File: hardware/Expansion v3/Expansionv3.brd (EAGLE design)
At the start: 89.2 x 36.7 mm, 44 parts, among them IC1 PIC18F2480-I/SP, J1 USB1035-XX-X-X-X-B_REVE, T1 BC547, T2 BC547, T3 BC547, T4 BC547, U1 IR3315, U2 IR3315, U3 IR3315, U4 IR3315

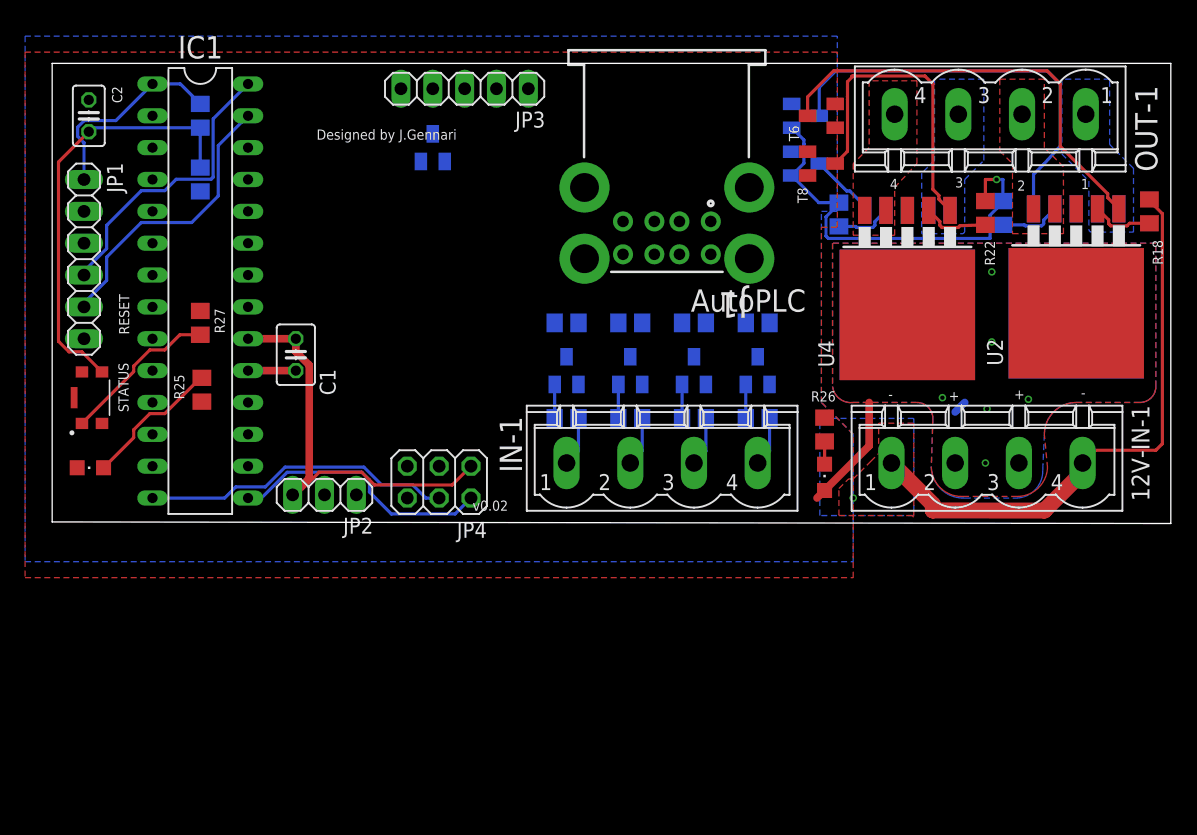
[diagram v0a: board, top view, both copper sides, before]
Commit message: Added ext board
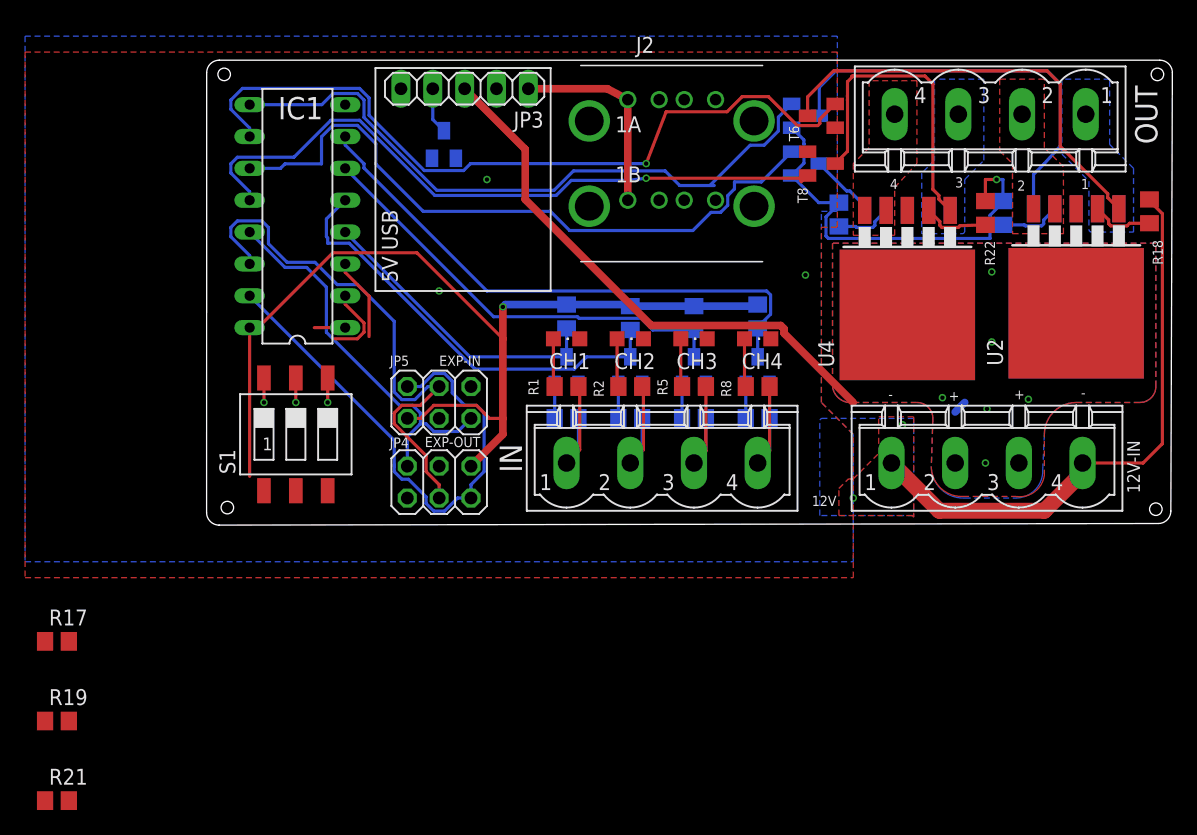
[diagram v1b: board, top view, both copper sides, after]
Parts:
- removed C1: 0.1uF, resistor:C025-030X050
- removed C2: 100nF, resistor:C025-025X050
- removed J1: USB1035-XX-X-X-X-B_REVE, USB1035-XX-X-X-X-B_REVE:GCT_USB1035-XX-X-X-X-B_REVE
- removed JP1: ICSP, pinhead:1X06
- removed JP2: 5V REG, pinhead:1X03
- removed LED10: (no value), led:CHIPLED_0805
- removed LED9: STATUS, led:CHIPLED_0805
- removed R24, R3: 10k, resistor:R0805
- removed R25: 150R, resistor:R0805
- removed R26: (no value), resistor:R0805
- removed R27: 100R, resistor:R0805
- added J2: (no value), InputOutputIO (rev17e):614008235023
- added JP5: (no value), pinhead:2X03
- added LED1, LED2, LED3, LED5: (no value), led:CHIPLED_0805
- added R1, R17, R19, R2, R21, R5, R8: (no value), resistor:R0805
- IC1: value PIC18F2480-I/SP -> PCF8574P; device microchip:DIL28-3 -> micro-philips:DIL16
- S1: value KMR421GULCLFS -> SWS003; device KMR421GULCLFS:SW_KMR421GULCLFS -> smd-special:SMS-003
- moved S1 16.5 mm to (43.2, 20.3), turned to 0 degrees
- moved IC1 9.78 mm to (43.3, 37.7), turned to 90 degrees
- moved T9 0.92 mm to (55.0, 43.4)
- moved R15 0.51 mm to (80.0, 29.7), turned to 270 degrees
- moved R6 0.51 mm to (64.8, 29.7), turned to 270 degrees
- moved R12 0.38 mm to (74.9, 29.6), turned to 270 degrees
- moved R9 0.38 mm to (69.8, 29.6), turned to 270 degrees
- renumbered 12V-IN-1 to 12V-IN, IN-1 to IN, OUT-1 to OUT
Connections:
- net OUT-1-1 renamed OUT-1
- net OUT-1-2 renamed OUT-2
- net OUT-1-3 renamed OUT-3
- net OUT-1-4 renamed OUT-4
- net SIGOUT-1-5 renamed SIGOUT-5
- removed net 12V-1: 12V-IN.2, 12V-IN.3, JP2.1, JP3.3, LED10.A, U1.6, U2.6, U3.6, U4.6
- removed net IN-1-1: IN.1, R4.1
- removed net IN-1-2: IN.2, R7.1
- removed net IN-1-3: IN.3, R10.1
- removed net IN-1-4: IN.4, R13.1
- removed net MCLR: IC1.1, JP1.1, R3.1
- removed net N$1: C2.1, R24.1, R3.2, S1.3
- removed net N$2: R27.2, S1.1
- removed net N$24: LED9.A, R25.2
- removed net N$25: LED10.C, R26.1
- removed net OUT-1-5: J1.1A, J1.1B, JP3.1
- removed net PGC: IC1.27, JP1.5
- removed net PGD: IC1.28, JP1.4
- removed net PGM: JP1.6
- removed net SIGIN-1-1: IC1.17, R6.2, T1.C
- removed net SIGIN-1-2: IC1.18, R9.2, T2.C
- removed net SIGIN-1-3: IC1.21, R12.2, T3.C
- removed net SIGIN-1-4: IC1.22, R15.2, T4.C
- removed net SIGOUT-1-1: IC1.5, T5.B
- removed net SIGOUT-1-2: IC1.4, T6.B
- removed net SIGOUT-1-3: IC1.3, T7.B
- removed net SIGOUT-1-4: IC1.2, T8.B
- removed net STATUS_LED: IC1.12, R25.1
- new net 12V: 12V-IN.2, 12V-IN.3, JP3.3, U1.6, U2.6, U3.6, U4.6
- new net A0: IC1.1, R21.2, S1.1
- new net A1: IC1.2, R19.2, S1.2
- new net A2: IC1.3, R17.2, S1.3
- new net IN-1: IN.1, R1.1, R4.1
- new net IN-2: IN.2, R2.1, R7.1
- new net IN-3: IN.3, R10.1, R5.1
- new net IN-4: IN.4, R13.1, R8.1
- new net INT: IC1.13, JP4.5, JP5.5
- new net N$3: LED5.A, R1.2
- new net N$5: LED1.A, R2.2
- new net N$7: LED2.A, R5.2
- new net N$9: LED3.A, R8.2
- new net OUT-5: J2.A1, J2.B1, JP3.1
- new net SIGIN-1: IC1.4, R6.2, T1.C
- new net SIGIN-2: IC1.5, R9.2, T2.C
- new net SIGIN-3: IC1.6, R12.2, T3.C
- new net SIGIN-4: IC1.7, R15.2, T4.C
- new net SIGOUT-1: IC1.9, T5.B
- new net SIGOUT-2: IC1.10, T6.B
- new net SIGOUT-3: IC1.11, T7.B
- new net SIGOUT-4: IC1.12, T8.B
- net GND: now also J2.A4, J2.B4, J2.SHELL, J2.SHELL1, J2.SHELL2, J2.SHELL3, JP5.3, LED1.C, LED2.C, LED3.C, LED5.C, R17.1, R19.1, R21.1; no longer C1.2, C2.2, IC1.19, J1.10, J1.11, J1.12, J1.4A, J1.4B, J1.9, JP1.3, JP2.2, LED9.C, R26.2, R27.1, S1.5
- net SCL: now also JP5.4
- net SDA: now also JP5.2
- net VCC: now also IC1.16, JP5.1, S1.4, S1.5, S1.6; no longer C1.1, IC1.20, JP1.2, JP2.3, R24.2
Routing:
- net SIGOUT-2: track 0.00 -> 61.1 mm, vias 0 -> 1
- net SIGOUT-4: track 0.00 -> 54.4 mm, vias 0 -> 1
- net SIGOUT-3: track 0.00 -> 53.7 mm
- net VCC: track 33.3 -> 86.0 mm, vias 0 -> 4
- net SIGOUT-1: track 0.00 -> 52.4 mm
- net SIGIN-4: track 0.00 -> 45.1 mm
- net 12V: track 0.00 -> 45.0 mm, vias 0 -> 6
- net SIGIN-3: track 0.00 -> 35.3 mm
- net SIGIN-2: track 0.00 -> 34.9 mm
- net N$1: track 34.4 -> 0.00 mm
- net INT: track 0.00 -> 31.1 mm
- net SIGIN-1: track 0.00 -> 24.0 mm
- net PGD: track 23.4 -> 0.00 mm
- net PGC: track 23.0 -> 0.00 mm
- net SDA: track 21.1 -> 42.6 mm
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- added copper zone on layer 1, net 12V
- added copper zone on layer 16, net 12V
- removed copper zone on layer 1, net 12V-1
- removed copper zone on layer 16, net 12V-1
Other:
- board size 89.2 x 36.7 mm -> 77 x 37.1 mm
- board text added: "12V"
- board text added: "CH1"
- board text added: "CH2"
- board text added: "CH3"
- board text added: "CH4"
- board text added: "EXP-IN"
- board text added: "EXP-OUT"
- board text removed: "AutoPLC"
- board text removed: "Designed by J.Gennari"
- board text removed: "RESET"
- board text removed: "STATUS"
- board text removed: "v0.02"
